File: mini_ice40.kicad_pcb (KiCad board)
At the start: 2 copper layers, 2 parts

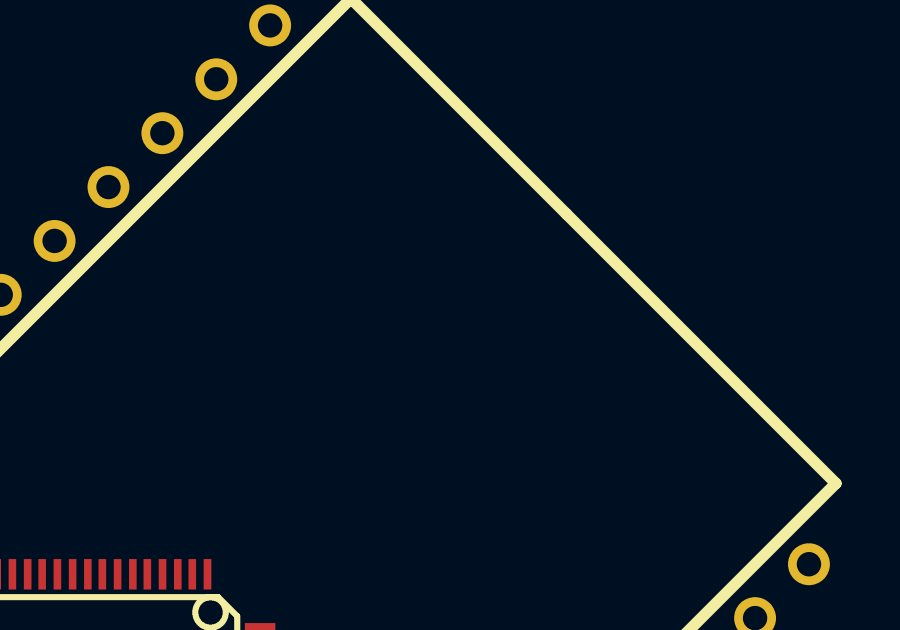
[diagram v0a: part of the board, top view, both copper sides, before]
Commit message: ** Switched regulators
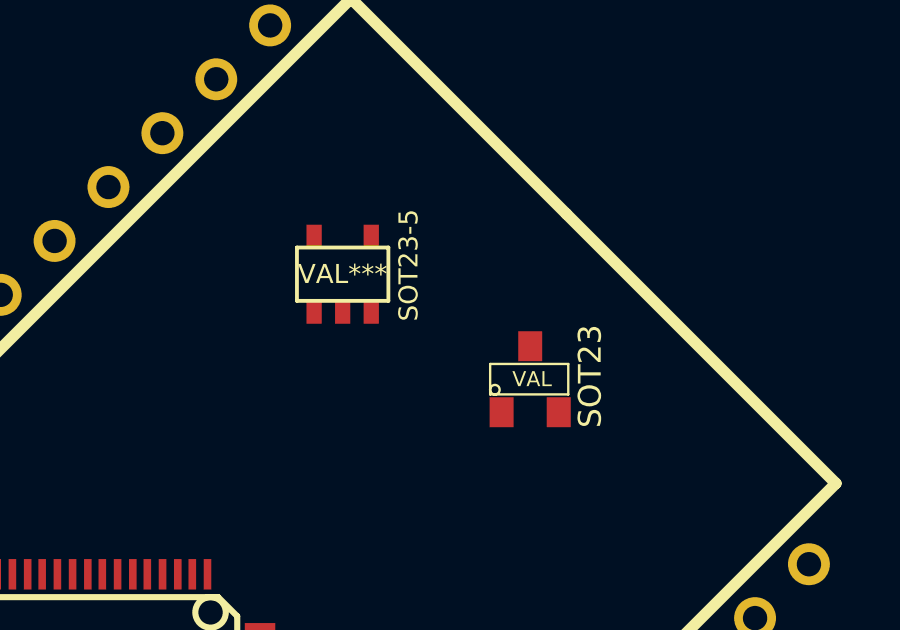
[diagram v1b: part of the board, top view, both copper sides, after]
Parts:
- added SOT23: VAL, SOT23, F.Cu at (110.2, 37.2)
- added SOT23-5: VAL***, SOT23-5, F.Cu at (104.0, 33.8)
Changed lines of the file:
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@@
     (tracks 0)
     (zones 0)
-    (modules 2)
+    (modules 4)
     (nets 1)
   )
@@
     )
   )
+  (module SOT23-5 (layer F.Cu)
+    (at 104 33.75)
+    (attr smd)
+    (fp_text reference SOT23-5 (at 2.19964 -0.29972 90) (layer F.SilkS)
+      (effects (font (size 0.635 0.635) (thickness 0.127)))
+    )
+    (fp_text value VAL*** (at 0 0) (layer F.SilkS)
+      (effects (font (size 0.635 0.635) (thickness 0.127)))
+    )
+    (fp_line (start 1.524 -0.889) (end 1.524 0.889) (layer F.SilkS) (width 0.127))
+    (fp_line (start 1.524 0.889) (end -1.524 0.889) (layer F.SilkS) (width 0.127))
+    (fp_line (start -1.524 0.889) (end -1.524 -0.889) (layer F.SilkS) (width 0.127))
+    (fp_line (start -1.524 -0.889) (end 1.524 -0.889) (layer F.SilkS) (width 0.127))
+    (pad 1 smd rect (at -0.9525 1.27) (size 0.508 0.762)
+      (layers F.Cu F.Paste F.Mask)
+    )
+    (pad 3 smd rect (at 0.9525 1.27) (size 0.508 0.762)
+      (layers F.Cu F.Paste F.Mask)
+    )
+    (pad 5 smd rect (at -0.9525 -1.27) (size 0.508 0.762)
+      (layers F.Cu F.Paste F.Mask)
+    )
+    (pad 2 smd rect (at 0 1.27) (size 0.508 0.762)
+      (layers F.Cu F.Paste F.Mask)
+    )
+    (pad 4 smd rect (at 0.9525 -1.27) (size 0.508 0.762)
+      (layers F.Cu F.Paste F.Mask)
+    )
+    (model smd/SOT23_5.wrl
+      (at (xyz 0 0 0))
+      (scale (xyz 0.1 0.1 0.1))
+      (rotate (xyz 0 0 0))
+    )
+  )
+  (module SOT23 (layer F.Cu)
+    (at 110.25 37.25)
+    (tags SOT23)
+    (fp_text reference SOT23 (at 1.99898 -0.09906 90) (layer F.SilkS)
+      (effects (font (size 0.762 0.762) (thickness 0.11938)))
+    )
+    (fp_text value VAL (at 0.0635 0) (layer F.SilkS)
+      (effects (font (size 0.50038 0.50038) (thickness 0.09906)))
+    )
+    (fp_circle (center -1.17602 0.35052) (end -1.30048 0.44958) (layer F.SilkS) (width 0.07874))
+    (fp_line (start 1.27 -0.508) (end 1.27 0.508) (layer F.SilkS) (width 0.07874))
+    (fp_line (start -1.3335 -0.508) (end -1.3335 0.508) (layer F.SilkS) (width 0.07874))
+    (fp_line (start 1.27 0.508) (end -1.3335 0.508) (layer F.SilkS) (width 0.07874))
+    (fp_line (start -1.3335 -0.508) (end 1.27 -0.508) (layer F.SilkS) (width 0.07874))
+    (pad 3 smd rect (at 0 -1.09982) (size 0.8001 1.00076)
+      (layers F.Cu F.Paste F.Mask)
+    )
+    (pad 2 smd rect (at 0.9525 1.09982) (size 0.8001 1.00076)
+      (layers F.Cu F.Paste F.Mask)
+    )
+    (pad 1 smd rect (at -0.9525 1.09982) (size 0.8001 1.00076)
+      (layers F.Cu F.Paste F.Mask)
+    )
+    (model smd\SOT23_3.wrl
+      (at (xyz 0 0 0))
+      (scale (xyz 0.4 0.4 0.4))
+      (rotate (xyz 0 0 180))
+    )
+  )

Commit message: ** Laid out PCB
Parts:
- removed ?: , DIP-40__1000
- removed SOT23: VAL, SOT23
- removed SOT23-5: VAL***, SOT23-5
- removed iCE40HX1K: VQ100, VQFP100
- added C1: 1u, Capacitors_SMD:C_0805_HandSoldering, B.Cu at (101.3, 33.5)
- added C10: 0u1, Capacitors_SMD:C_0603_HandSoldering, B.Cu at (93.0, 44.7)
- added C11: 0u1, Capacitors_SMD:C_0603_HandSoldering, B.Cu at (91.1, 58.3)
- added C12: 0u1, Capacitors_SMD:C_0603_HandSoldering, B.Cu at (89.0, 44.7)
- added C13: 0u1, Capacitors_SMD:C_0603_HandSoldering, B.Cu at (100.2, 49.5)
- added C14: 0u1, Capacitors_SMD:C_0603_HandSoldering, B.Cu at (97.0, 44.7)
- added C15: 0u1, Capacitors_SMD:C_0603_HandSoldering, B.Cu at (86.7, 48.0)
- added C16: 0u1, Capacitors_SMD:C_0603_HandSoldering, B.Cu at (86.7, 50.0)
- added C17: 0u1, Capacitors_SMD:C_0603_HandSoldering, B.Cu at (94.5, 44.7)
- added C18: 0u1, Capacitors_SMD:C_0603_HandSoldering, B.Cu at (100.2, 57.0)
- added C19: 0u1, Capacitors_SMD:C_0603_HandSoldering, B.Cu at (92.5, 58.3)
- added C2: 1u, Capacitors_SMD:C_0805_HandSoldering, B.Cu at (105.3, 33.4)
- added C3: 1u, Capacitors_SMD:C_0805_HandSoldering, B.Cu at (107.7, 33.4)
- added C4: 0u1, Capacitors_SMD:C_0603_HandSoldering, B.Cu at (85.0, 62.7)
- added C5: 0u1, Capacitors_SMD:C_0603_HandSoldering, B.Cu at (90.4, 63.5)
- added C6: 0u1, Capacitors_SMD:C_0603_HandSoldering, B.Cu at (86.7, 57.5)
- added C7: 0u1, Capacitors_SMD:C_0603_HandSoldering, B.Cu at (100.2, 51.6)
- added C8: 0u1, Capacitors_SMD:C_0603_HandSoldering, B.Cu at (86.7, 51.4)
- added C9: 0u1, Capacitors_SMD:C_0603_HandSoldering, B.Cu at (95.5, 58.3)
- added D1: 1N4448WQ-7-F, Diodes_SMD:SOD-123, F.Cu at (75.2, 60.3)
- added DDONE1: SML-LX1206GC-TR1, LEDs:LED_1206, F.Cu at (103.4, 38.7)
- added FPGA1: ICE40HX1K-VQ100, mini_ice40:VQFP100, F.Cu at (93.5, 51.5)
- added OSC1: ASDMB-26MHZ-LC, mini_ice40:2MMx2MM5, F.Cu at (90.4, 63.5)
- added P1: CONN_01X20, Pin_Headers:Pin_Header_Straight_1x20, F.Cu at (101.6, 25.4)
- added P2: CONN_01X04, Pin_Headers:Pin_Header_Straight_1x06, F.Cu at (72.4, 64.3)
- added P3: CONN_01X20, Pin_Headers:Pin_Header_Straight_1x20, F.Cu at (85.4, 77.5)
- added Q1: 2N7002LT1G, TO_SOT_Packages_SMD:SOT-23_Handsoldering, F.Cu at (112.8, 39.1)
- added R1: 330, Resistors_SMD:R_0603_HandSoldering, F.Cu at (108.5, 38.7)
- added R2: 10K, Resistors_SMD:R_0603_HandSoldering, F.Cu at (107.8, 42.2)
- added R3: 10K, Resistors_SMD:R_0603_HandSoldering, F.Cu at (82.2, 56.9)
- added REG1: AP7312-1233W6-7, TO_SOT_Packages_SMD:SOT-23-6, F.Cu at (106.4, 33.4)
- added RST1: SW_PUSH, Buttons_Switches_SMD:SW_SPST_B3U-1000P, F.Cu at (103.1, 42.2)
- added SPI_FLASH1: AT25SF041-SSHD-B, SMD_Packages:SOIC-8-N, F.Cu at (81.8, 63.2)
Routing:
- net +3V3: track 0.00 -> 163.9 mm, vias 0 -> 12
- net GND: track 0.00 -> 106.9 mm, vias 0 -> 24
- net +1V2: track 0.00 -> 97.5 mm, vias 0 -> 5
- net Net-(FPGA1-Pad43): track 0.00 -> 34.3 mm, vias 0 -> 2
- net Net-(FPGA1-Pad44): track 0.00 -> 30.1 mm, vias 0 -> 4
- net Net-(FPGA1-Pad48): track 0.00 -> 27.6 mm, vias 0 -> 4
- net Net-(FPGA1-Pad45): track 0.00 -> 26.1 mm, vias 0 -> 2
- net Net-(FPGA1-Pad49): track 0.00 -> 25.0 mm, vias 0 -> 2
- net Net-(FPGA1-Pad46): track 0.00 -> 24.4 mm, vias 0 -> 4
- net Net-(FPGA1-Pad63): track 0.00 -> 23.1 mm
- net Net-(FPGA1-Pad89): track 0.00 -> 21.4 mm
- net Net-(FPGA1-Pad40): track 0.00 -> 21.2 mm
- net Net-(C4-Pad1): track 0.00 -> 20.4 mm, vias 0 -> 2
- net Net-(FPGA1-Pad64): track 0.00 -> 19.9 mm
- net Net-(FPGA1-Pad87): track 0.00 -> 19.3 mm
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- added copper zone on B.Cu, net GND
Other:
- net class Default: clearance 0.254 -> 0.2; trace_width 0.254 -> 0.18; via_dia 0.889 -> 0.72
- net class Thick added: clearance 0.2, trace_width 0.254, via_dia 0.72, via_drill 0.635
- rule trace_clearance: 0.254 -> 0.2
- rule trace_min: 0.254 -> 0.15
- rule via_min_size: 0.889 -> 0.72

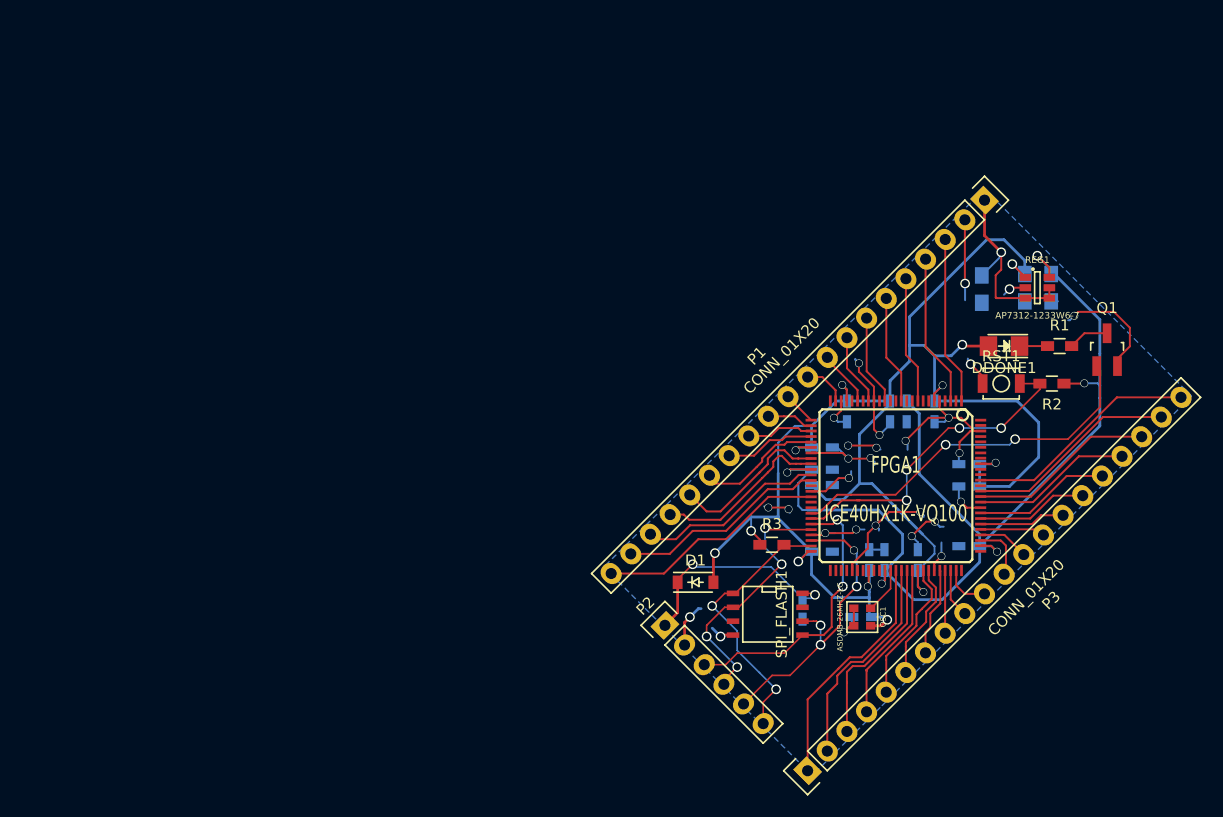
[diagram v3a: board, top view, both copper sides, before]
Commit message: ** Shorter PCB to keep <5cm
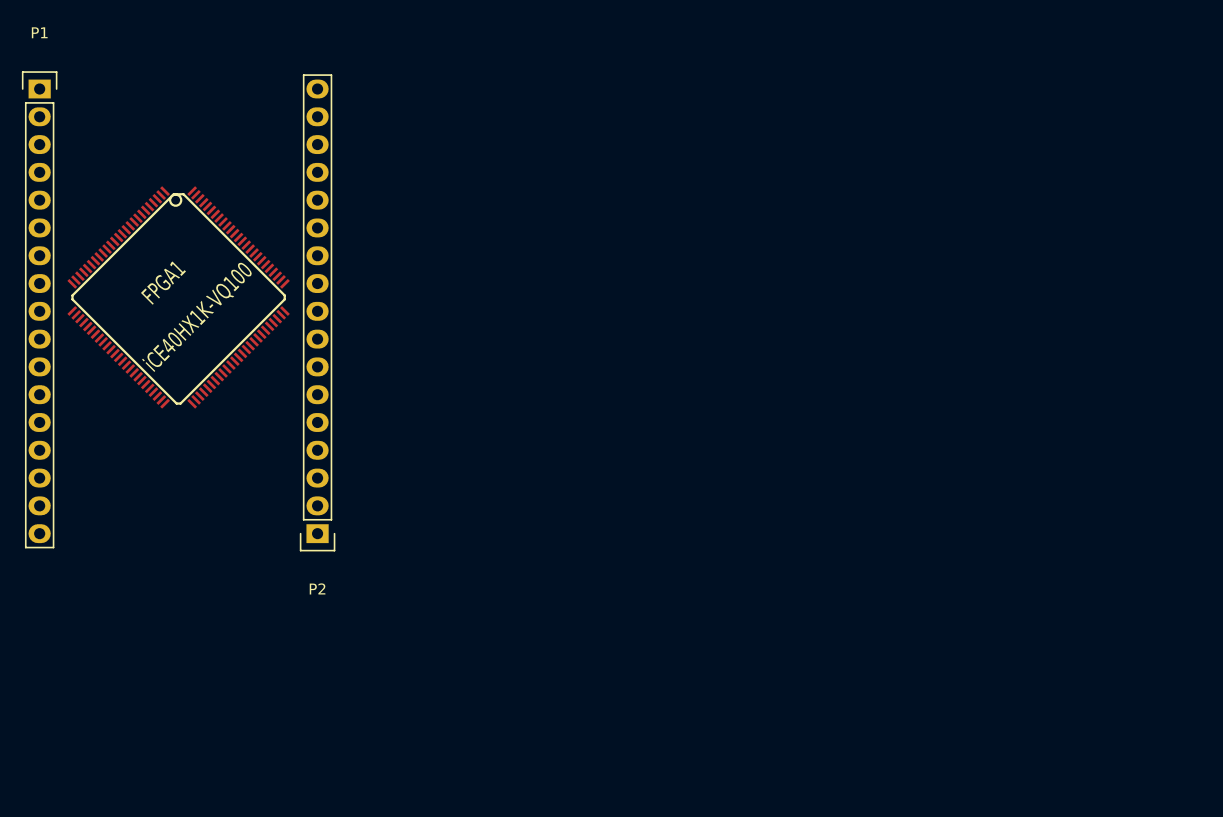
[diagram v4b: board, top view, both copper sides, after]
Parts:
- removed C1, C2, C3: 1u, Capacitors_SMD:C_0805_HandSoldering
- removed C10, C11, C12, C13, C14, C15, C16, C17, C18, C19, C4, C5, C6, C7, C8, C9: 0u1, Capacitors_SMD:C_0603_HandSoldering
- removed D1: 1N4448WQ-7-F, Diodes_SMD:SOD-123
- removed DDONE1: SML-LX1206GC-TR1, LEDs:LED_1206
- removed OSC1: ASDMB-26MHZ-LC, mini_ice40:2MMx2MM5
- removed P3: CONN_01X20, Pin_Headers:Pin_Header_Straight_1x20
- removed Q1: 2N7002LT1G, TO_SOT_Packages_SMD:SOT-23_Handsoldering
- removed R1: 330, Resistors_SMD:R_0603_HandSoldering
- removed R2, R3: 10K, Resistors_SMD:R_0603_HandSoldering
- removed REG1: AP7312-1233W6-7, TO_SOT_Packages_SMD:SOT-23-6
- removed RST1: SW_PUSH, Buttons_Switches_SMD:SW_SPST_B3U-1000P
- removed SPI_FLASH1: AT25SF041-SSHD-B, SMD_Packages:SOIC-8-N
- FPGA1: value ICE40HX1K-VQ100 -> iCE40HX1K-VQ100
- P1: value CONN_01X20 -> Pin_Header_Straight_1x18; footprint Pin_Headers:Pin_Header_Straight_1x20 -> Pin_Headers:Pin_Header_Straight_1x17
- P2: value CONN_01X04 -> Pin_Header_Straight_1x18; footprint Pin_Headers:Pin_Header_Straight_1x06 -> Pin_Headers:Pin_Header_Straight_1x17
- moved P1 87.0 mm to (15.2, 15.2), turned to 0 degrees
- moved FPGA1 67.8 mm to (27.9, 34.3), turned to 45 degrees
- moved P2 32.8 mm to (40.6, 55.9), turned to 180 degrees
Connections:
- FPGA1 pad 1: Net-(FPGA1-Pad1) -> (no net)
- FPGA1 pad 10: Net-(FPGA1-Pad10) -> (no net)
- FPGA1 pad 100: Net-(FPGA1-Pad100) -> (no net)
- FPGA1 pad 11: +1V2 -> (no net)
- FPGA1 pad 12: Net-(FPGA1-Pad12) -> (no net)
- FPGA1 pad 13: Net-(FPGA1-Pad13) -> (no net)
- FPGA1 pad 14: +3V3 -> (no net)
- FPGA1 pad 15: Net-(FPGA1-Pad15) -> (no net)
- FPGA1 pad 16: Net-(FPGA1-Pad16) -> (no net)
- FPGA1 pad 17: GND -> (no net)
- FPGA1 pad 18: Net-(FPGA1-Pad18) -> (no net)
- FPGA1 pad 19: Net-(FPGA1-Pad19) -> (no net)
- FPGA1 pad 2: Net-(FPGA1-Pad2) -> (no net)
- FPGA1 pad 20: Net-(FPGA1-Pad20) -> (no net)
- FPGA1 pad 21: Net-(FPGA1-Pad21) -> (no net)
- FPGA1 pad 22: +3V3 -> (no net)
- FPGA1 pad 23: GND -> (no net)
- FPGA1 pad 24: Net-(FPGA1-Pad24) -> (no net)
- FPGA1 pad 25: Net-(FPGA1-Pad25) -> (no net)
- FPGA1 pad 26: Net-(FPGA1-Pad26) -> (no net)
- FPGA1 pad 27: Net-(FPGA1-Pad27) -> (no net)
- FPGA1 pad 28: Net-(FPGA1-Pad28) -> (no net)
- FPGA1 pad 29: Net-(FPGA1-Pad29) -> (no net)
- FPGA1 pad 3: Net-(FPGA1-Pad3) -> (no net)
- FPGA1 pad 30: Net-(FPGA1-Pad30) -> (no net)
- FPGA1 pad 31: +3V3 -> (no net)
- FPGA1 pad 32: GND -> (no net)
- FPGA1 pad 33: Net-(FPGA1-Pad33) -> (no net)
- FPGA1 pad 34: Net-(FPGA1-Pad34) -> (no net)
- FPGA1 pad 35: +1V2 -> (no net)
- FPGA1 pad 36: Net-(FPGA1-Pad36) -> (no net)
- FPGA1 pad 37: Net-(FPGA1-Pad37) -> (no net)
- FPGA1 pad 38: +3V3 -> (no net)
- FPGA1 pad 39: GND -> (no net)
- FPGA1 pad 4: Net-(FPGA1-Pad4) -> (no net)
- FPGA1 pad 40: Net-(FPGA1-Pad40) -> (no net)
- FPGA1 pad 41: Net-(FPGA1-Pad41) -> (no net)
- FPGA1 pad 42: Net-(FPGA1-Pad42) -> (no net)
- FPGA1 pad 43: Net-(FPGA1-Pad43) -> (no net)
- FPGA1 pad 44: Net-(FPGA1-Pad44) -> (no net)
- FPGA1 pad 45: Net-(FPGA1-Pad45) -> (no net)
- FPGA1 pad 46: Net-(FPGA1-Pad46) -> (no net)
- FPGA1 pad 47: GND -> (no net)
- FPGA1 pad 48: Net-(FPGA1-Pad48) -> (no net)
- FPGA1 pad 49: Net-(FPGA1-Pad49) -> (no net)
- FPGA1 pad 5: GND -> (no net)
- FPGA1 pad 50: +3V3 -> (no net)
- FPGA1 pad 51: Net-(FPGA1-Pad51) -> (no net)
- FPGA1 pad 52: Net-(FPGA1-Pad52) -> (no net)
- FPGA1 pad 53: Net-(FPGA1-Pad53) -> (no net)
- FPGA1 pad 54: Net-(FPGA1-Pad54) -> (no net)
- FPGA1 pad 55: GND -> (no net)
- FPGA1 pad 56: Net-(FPGA1-Pad56) -> (no net)
- FPGA1 pad 57: Net-(FPGA1-Pad57) -> (no net)
- FPGA1 pad 58: +3V3 -> (no net)
- FPGA1 pad 59: Net-(FPGA1-Pad59) -> (no net)
- FPGA1 pad 6: +3V3 -> (no net)
- FPGA1 pad 60: Net-(FPGA1-Pad60) -> (no net)
- FPGA1 pad 61: +1V2 -> (no net)
- FPGA1 pad 62: Net-(FPGA1-Pad62) -> (no net)
- FPGA1 pad 63: Net-(FPGA1-Pad63) -> (no net)
- FPGA1 pad 64: Net-(FPGA1-Pad64) -> (no net)
- FPGA1 pad 65: Net-(FPGA1-Pad65) -> (no net)
- FPGA1 pad 66: Net-(FPGA1-Pad66) -> (no net)
- FPGA1 pad 67: +3V3 -> (no net)
- FPGA1 pad 68: Net-(FPGA1-Pad68) -> (no net)
- FPGA1 pad 69: Net-(FPGA1-Pad69) -> (no net)
- FPGA1 pad 70: GND -> (no net)
- FPGA1 pad 71: Net-(FPGA1-Pad71) -> (no net)
- FPGA1 pad 72: Net-(FPGA1-Pad72) -> (no net)
- FPGA1 pad 73: Net-(FPGA1-Pad73) -> (no net)
- FPGA1 pad 74: Net-(FPGA1-Pad74) -> (no net)
- FPGA1 pad 77: +1V2 -> (no net)
- FPGA1 pad 78: Net-(FPGA1-Pad78) -> (no net)
- FPGA1 pad 79: Net-(FPGA1-Pad79) -> (no net)
- FPGA1 pad 80: Net-(FPGA1-Pad80) -> (no net)
- FPGA1 pad 81: Net-(FPGA1-Pad81) -> (no net)
- FPGA1 pad 82: Net-(FPGA1-Pad82) -> (no net)
- FPGA1 pad 83: Net-(FPGA1-Pad83) -> (no net)
- FPGA1 pad 84: GND -> (no net)
- FPGA1 pad 85: Net-(FPGA1-Pad85) -> (no net)
- FPGA1 pad 86: Net-(FPGA1-Pad86) -> (no net)
- FPGA1 pad 87: Net-(FPGA1-Pad87) -> (no net)
- FPGA1 pad 88: +3V3 -> (no net)
- FPGA1 pad 89: Net-(FPGA1-Pad89) -> (no net)
- FPGA1 pad 9: Net-(FPGA1-Pad9) -> (no net)
- FPGA1 pad 90: Net-(FPGA1-Pad90) -> (no net)
- FPGA1 pad 91: Net-(FPGA1-Pad91) -> (no net)
- FPGA1 pad 92: +3V3 -> (no net)
- FPGA1 pad 93: Net-(FPGA1-Pad93) -> (no net)
- FPGA1 pad 94: Net-(FPGA1-Pad94) -> (no net)
- FPGA1 pad 95: Net-(FPGA1-Pad95) -> (no net)
- FPGA1 pad 96: Net-(FPGA1-Pad96) -> (no net)
- FPGA1 pad 97: Net-(FPGA1-Pad97) -> (no net)
- FPGA1 pad 98: GND -> (no net)
- FPGA1 pad 99: Net-(FPGA1-Pad99) -> (no net)
- P1 pad 1: VCC -> (no net)
- P1 pad 10: Net-(FPGA1-Pad24) -> (no net)
- P1 pad 11: Net-(FPGA1-Pad26) -> (no net)
- P1 pad 12: Net-(FPGA1-Pad27) -> (no net)
- P1 pad 13: Net-(FPGA1-Pad28) -> (no net)
- P1 pad 14: Net-(FPGA1-Pad29) -> (no net)
- P1 pad 15: Net-(FPGA1-Pad30) -> (no net)
- P1 pad 16: Net-(FPGA1-Pad33) -> (no net)
- P1 pad 17: Net-(FPGA1-Pad34) -> (no net)
- P1 pad 2: GND -> (no net)
- P1 pad 3: Net-(FPGA1-Pad1) -> (no net)
- P1 pad 4: Net-(FPGA1-Pad3) -> (no net)
- P1 pad 5: Net-(FPGA1-Pad9) -> (no net)
- P1 pad 6: Net-(FPGA1-Pad12) -> (no net)
- P1 pad 7: Net-(FPGA1-Pad15) -> (no net)
- P1 pad 8: Net-(FPGA1-Pad18) -> (no net)
- P1 pad 9: Net-(FPGA1-Pad20) -> (no net)
- P2 pad 1: Net-(C4-Pad1) -> (no net)
- P2 pad 2: GND -> (no net)
- P2 pad 3: Net-(FPGA1-Pad45) -> (no net)
- P2 pad 4: Net-(FPGA1-Pad46) -> (no net)
- P2 pad 5: Net-(FPGA1-Pad48) -> (no net)
- P2 pad 6: Net-(FPGA1-Pad49) -> (no net)
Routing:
- net +3V3: track 163.9 -> 0.00 mm, vias 12 -> 0
- net GND: track 106.9 -> 0.00 mm, vias 24 -> 0
- net +1V2: track 97.5 -> 0.00 mm, vias 5 -> 0
- net Net-(FPGA1-Pad43): track 34.3 -> 0.00 mm, vias 2 -> 0
- net Net-(FPGA1-Pad44): track 30.1 -> 0.00 mm, vias 4 -> 0
- net Net-(FPGA1-Pad48): track 27.6 -> 0.00 mm, vias 4 -> 0
- net Net-(FPGA1-Pad45): track 26.1 -> 0.00 mm, vias 2 -> 0
- net Net-(FPGA1-Pad49): track 25.0 -> 0.00 mm, vias 2 -> 0
- net Net-(FPGA1-Pad46): track 24.4 -> 0.00 mm, vias 4 -> 0
- net Net-(FPGA1-Pad63): track 23.1 -> 0.00 mm
- net Net-(FPGA1-Pad89): track 21.4 -> 0.00 mm
- net Net-(FPGA1-Pad40): track 21.2 -> 0.00 mm
- net Net-(C4-Pad1): track 20.4 -> 0.00 mm, vias 2 -> 0
- net Net-(FPGA1-Pad64): track 19.9 -> 0.00 mm
- net Net-(FPGA1-Pad87): track 19.3 -> 0.00 mm
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- removed copper zone on B.Cu, net GND
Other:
- net class Default: trace_width 0.18 -> 0.25; via_dia 0.72 -> 0.6; via_drill 0.635 -> 0.4
- net class Thick removed
- rule trace_min: 0.15 -> 0.2
- rule via_min_drill: 0.508 -> 0.3
- rule via_min_size: 0.72 -> 0.4
